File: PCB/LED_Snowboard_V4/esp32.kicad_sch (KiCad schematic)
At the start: 29 parts

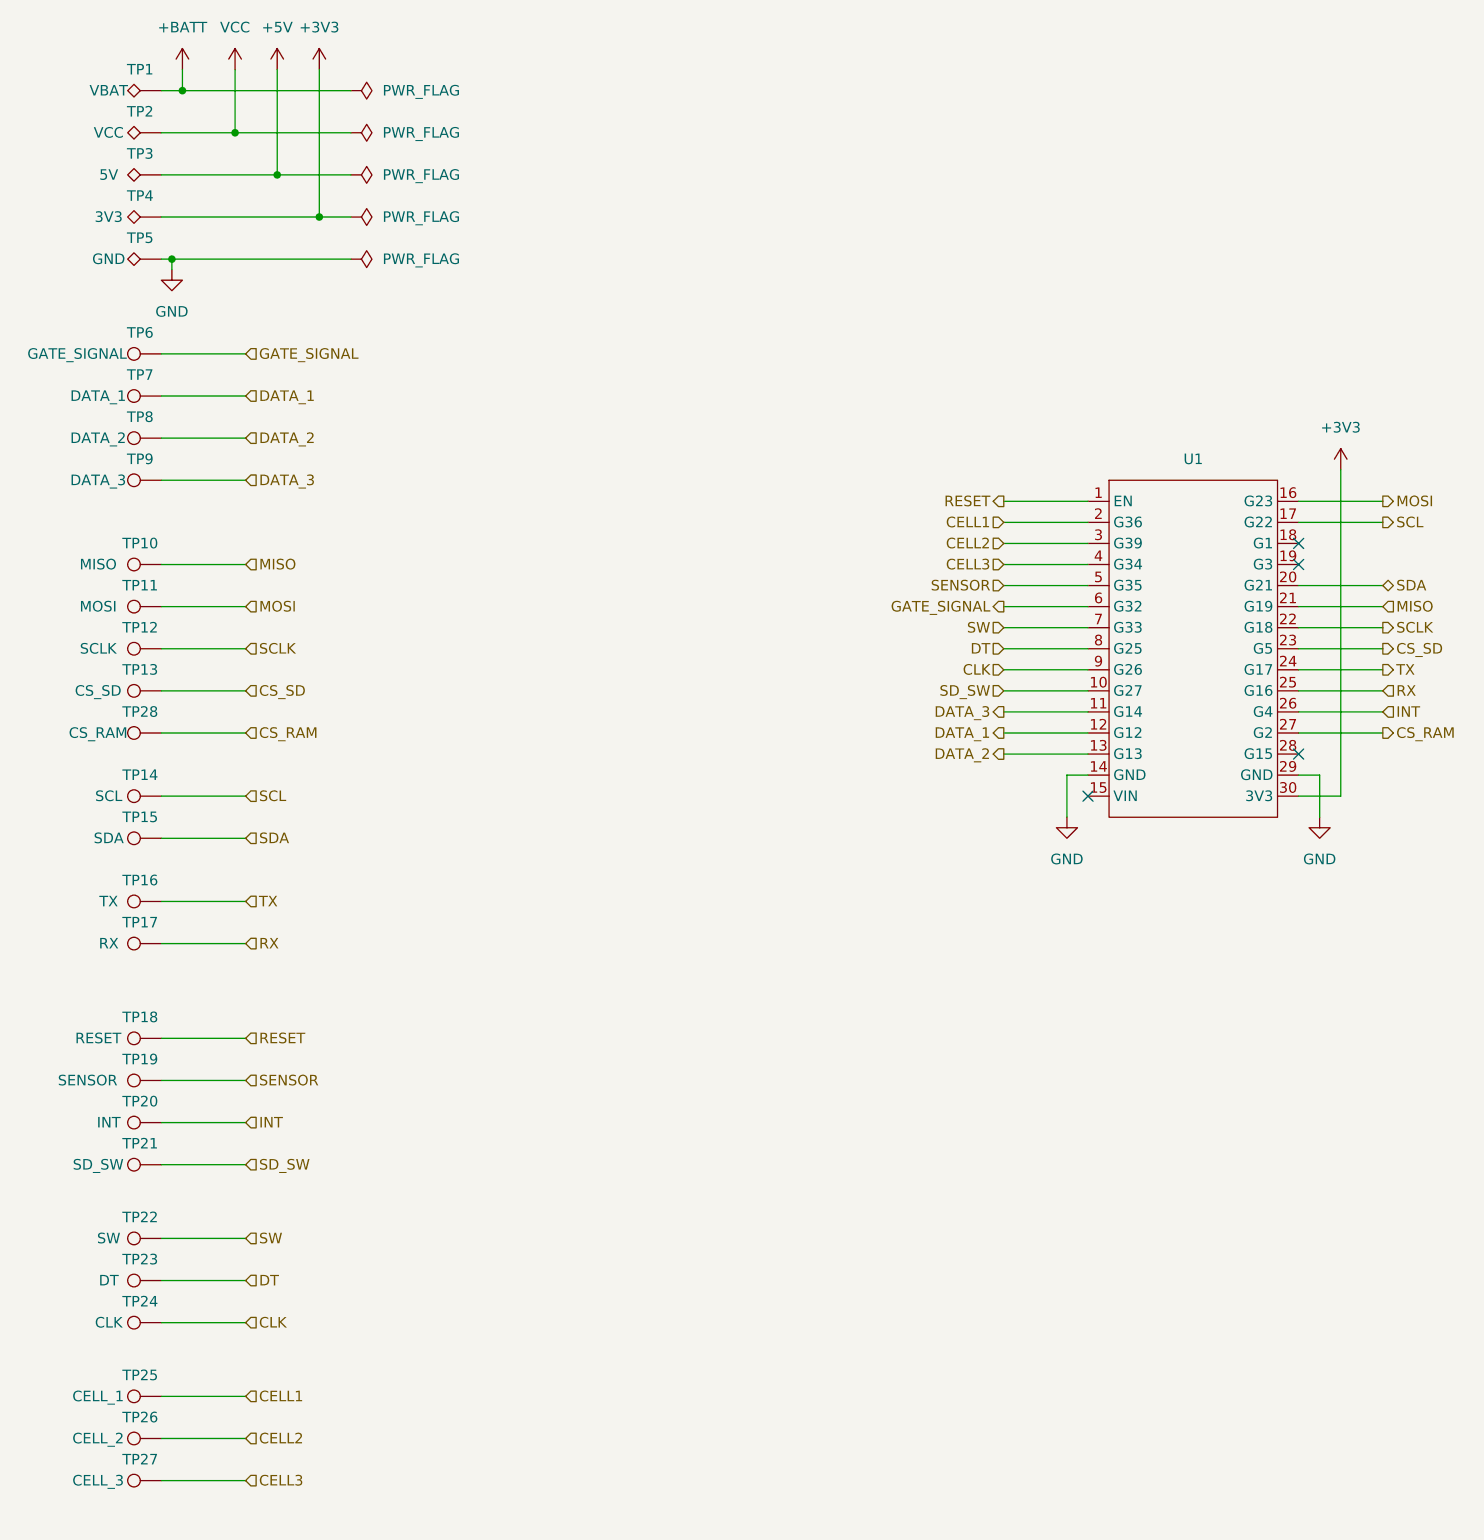
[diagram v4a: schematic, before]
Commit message: updated control pcb
updated to add high side switching as well as added voltage divider and adjusted layout
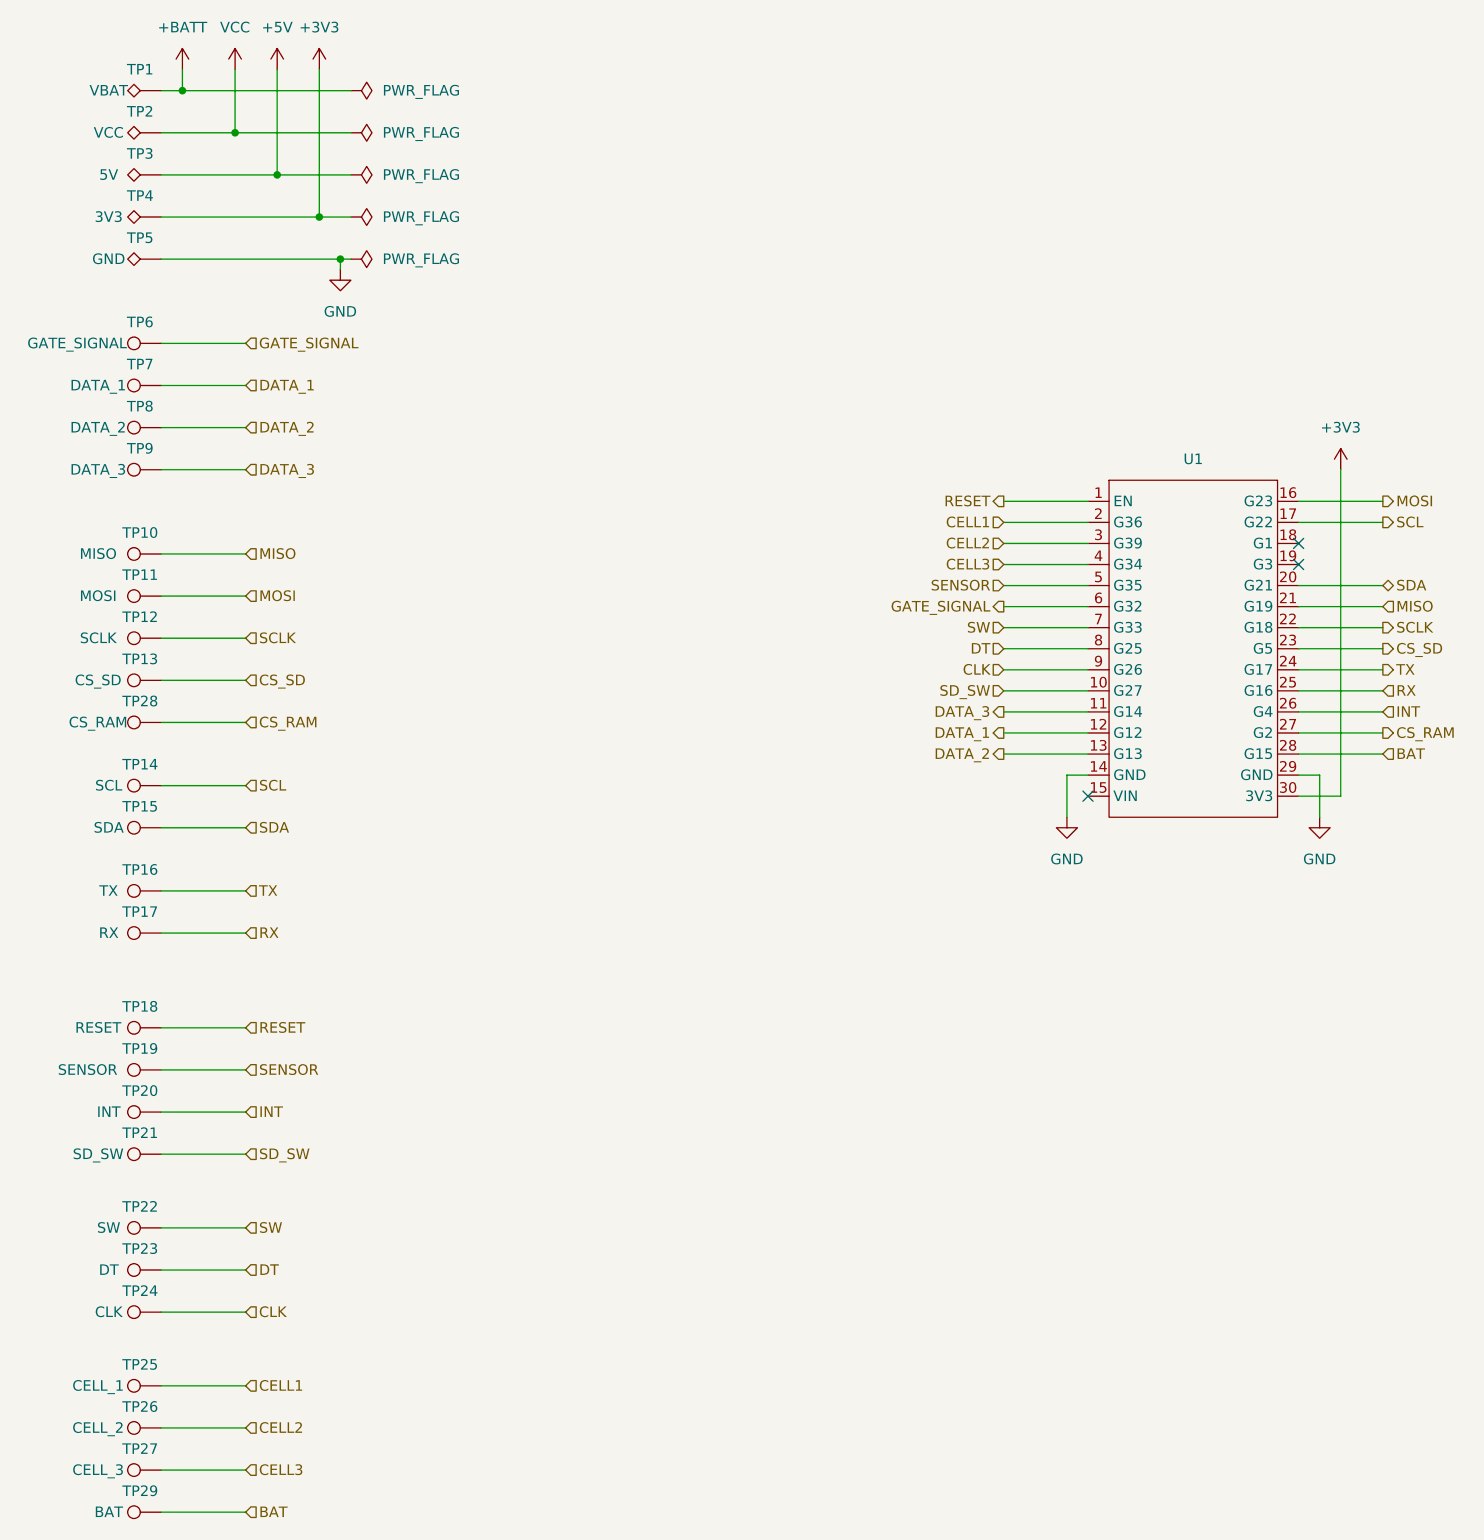
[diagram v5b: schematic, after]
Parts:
- added TP29: BAT, TestPoint:TestPoint_Pad_D1.5mm, symbol Connector:TestPoint
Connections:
- net BAT: now reaches U1.28 (G15)
- net BAT: now also TP29.1
- no-connect marks 4 -> 3
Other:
- moved on the sheet: TP10, TP11, TP12, TP13, TP14, TP15, TP16, TP17, TP18, TP19, TP20, TP21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
